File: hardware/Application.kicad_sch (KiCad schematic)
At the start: 0 parts

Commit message: Schematic updates: stm32 sheet
Signed-off-by: Connor Rigby <connorr@hey.com>
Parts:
- added C504, C505: C_0402_DNP, Capacitor_SMD:C_0402_1005Metric, symbol LCSC_Capacitor:C_0402_DNP
- added C505, C507, C50823, C50835, C50848, C511: C_0402_100nf_X7R, Capacitor_SMD:C_0402_1005Metric, symbol LCSC_Capacitor:C_0402_100nf_X7R
- added C509: C_0805_10u_X5R, Capacitor_SMD:C_0805_2012Metric, symbol LCSC_Capacitor:C_0805_10u_X5R
- added R502: R_0402_10k, Resistor_SMD:R_0402_1005Metric, symbol LCSC_Resistor:R_0402_10k
- added U501: STM32G431CBU6, LCSC_Microcontroller:UFQFPN-48_L7.0-W7.0-P0.50-BL-EP, symbol LCSC_Microcontroller:STM32G431CBU6
- added Y501: 32_Mhz, Crystal:Crystal_SMD_3225-4Pin_3.2x2.5mm, symbol LCSC_Crystal:32_Mhz
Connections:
- new net GND: U501.49 (EP)

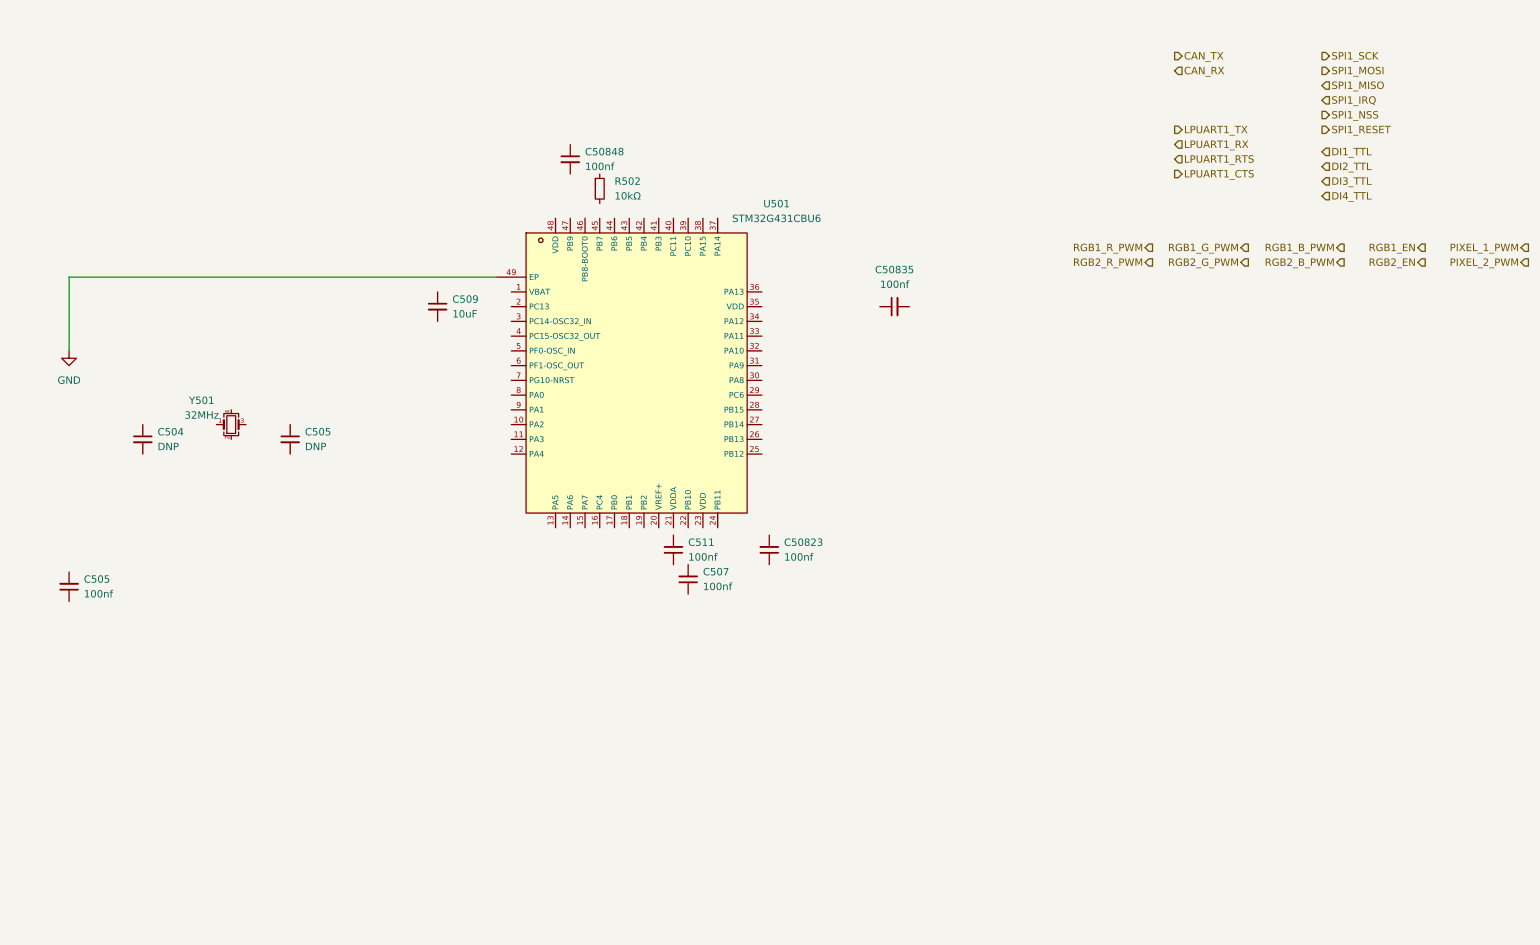
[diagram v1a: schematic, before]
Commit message: Schematic and layout Progress
Signed-off-by: Connor Rigby <connorr@hey.com>
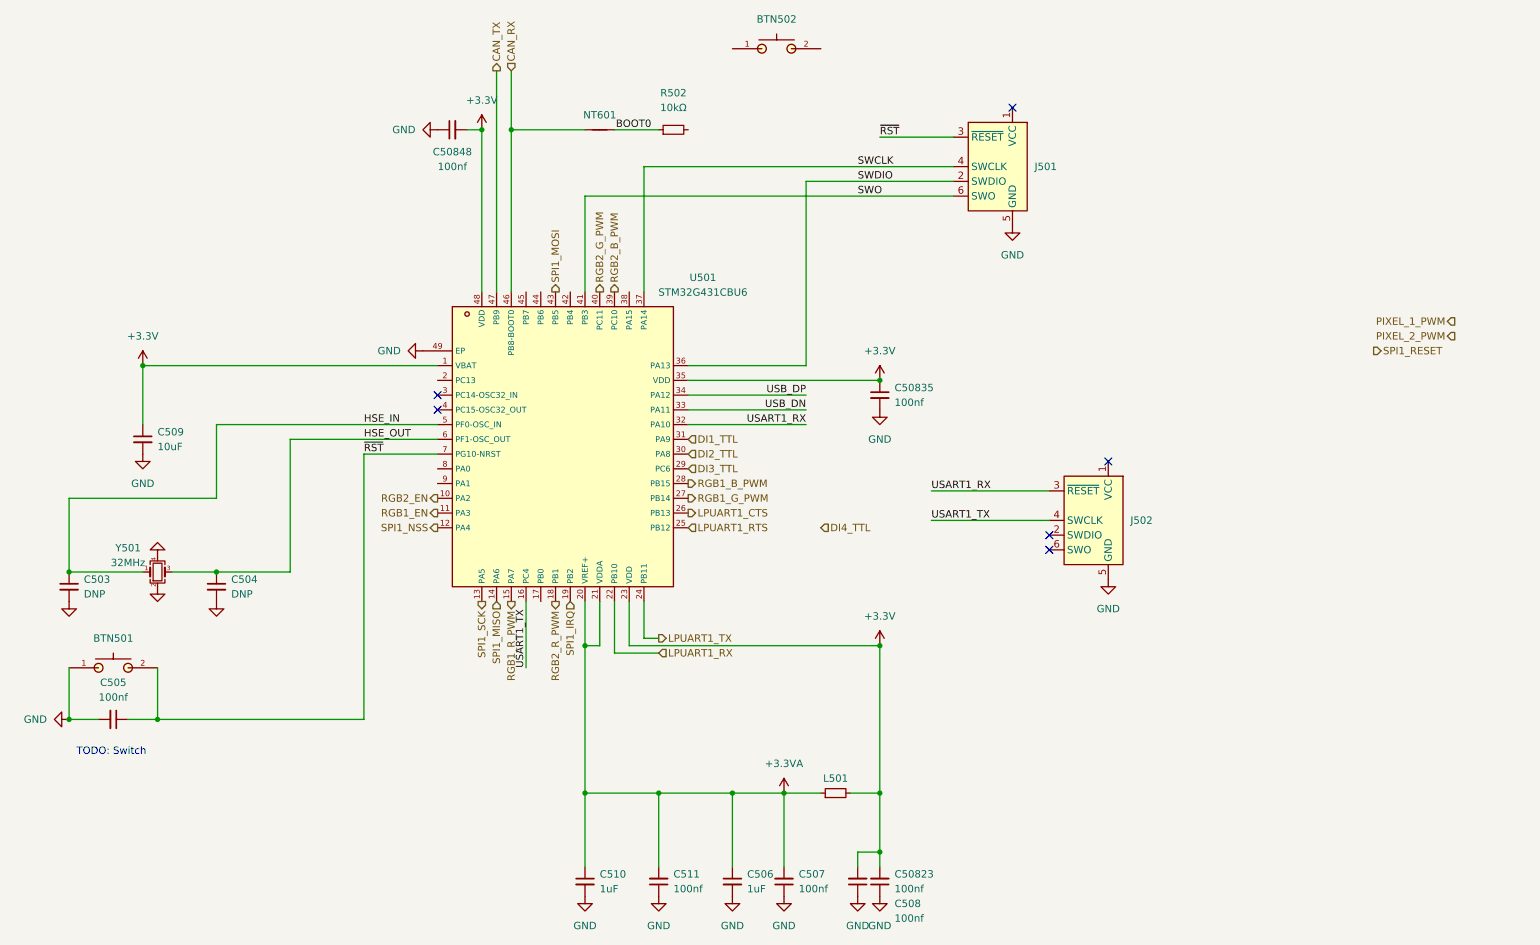
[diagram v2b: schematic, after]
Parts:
- added BTN501, BTN502: GT-TC029B-H025-L1N, Button:SW-SMD_L3.9-W3.0-P4.45, symbol LCSC_Tactile_Switch:GT-TC029B-H025-L1N
- added C506, C510: C_0402_1u_X5R, Capacitor_SMD:C_0402_1005Metric, symbol LCSC_Capacitor:C_0402_1u_X5R
- added C508: C_0402_100nf_X7R, Capacitor_SMD:C_0402_1005Metric, symbol LCSC_Capacitor:C_0402_100nf_X7R
- added J501: Conn_ARM_SWD_TagConnect_TC2030-NL, Connector:Tag-Connect_TC2030-IDC-NL_2x03_P1.27mm_Vertical, symbol Connector:Conn_ARM_SWD_TagConnect_TC2030-NL
- added J502: Conn_ARM_SWD_TagConnect_TC2030, Connector:Tag-Connect_TC2030-IDC-FP_2x03_P1.27mm_Vertical, symbol Connector:Conn_ARM_SWD_TagConnect_TC2030
- added L501: R_0402_DNP, Resistor_SMD:R_0402_1005Metric, symbol LCSC_Resistor:R_0402_DNP
- added NT601: NetTie_2, NetTie:NetTie-2_SMD_Pad0.5mm, symbol Device:NetTie_2
- renumbered C504 to C503, C505 to C504
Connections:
- net CAN_RX: now also U501.46 (PB8-BOOT0), NT601.1
- net CAN_TX: now also U501.47 (PB9)
- net DI1_TTL: now also U501.31 (PA9)
- net DI2_TTL: now also U501.30 (PA8)
- net DI3_TTL: now also U501.29 (PC6)
- net GND: now also C503.2, C504.2, C505.2, C507.1, C50823.1, C50835.2, C50848.1, C509.2, C511.1, Y501.2, Y501.4, BTN501.1, C506.2, C508.1, C510.2, J501.5 (GND), J502.5 (GND)
- net LPUART1_CTS: now also U501.26 (PB13)
- net LPUART1_RTS: now also U501.25 (PB12)
- net LPUART1_RX: now also U501.22 (PB10)
- net LPUART1_TX: now also U501.24 (PB11)
- net RGB1_B_PWM: now also U501.28 (PB15)
- net RGB1_EN: now also U501.11 (PA3)
- net RGB1_G_PWM: now also U501.27 (PB14)
- net RGB1_R_PWM: now also U501.15 (PA7)
- net RGB2_B_PWM: now also U501.39 (PC10)
- net RGB2_EN: now also U501.10 (PA2)
- net RGB2_G_PWM: now also U501.40 (PC11)
- net RGB2_R_PWM: now also U501.18 (PB1)
- net SPI1_IRQ: now also U501.19 (PB2)
- net SPI1_MISO: now also U501.14 (PA6)
- net SPI1_MOSI: now also U501.43 (PB5)
- net SPI1_NSS: now also U501.12 (PA4)
- net SPI1_SCK: now also U501.13 (PA5)
- net HSE_IN: now reaches Y501.1
- net HSE_IN: now also C503.1, U501.5 (PF0-OSC_IN)
- net HSE_OUT: now reaches Y501.3
- net HSE_OUT: now also C504.1, U501.6 (PF1-OSC_OUT)
- net +3.3VA: now reaches C507.2
- net +3.3VA: now also C511.2, U501.20 (VREF+), U501.21 (VDDA), C506.1, C510.1, L501.1
- net +3.3V: now reaches C50823.2
- net +3.3V: now also C50835.1, C50848.2, C509.1, U501.1 (VBAT), U501.23 (VDD), U501.35 (VDD), U501.48 (VDD), C508.2, L501.2
- net USART1_TX: now reaches U501.16 (PC4)
- net USART1_TX: now also J502.4 (SWCLK)
- net USART1_RX: now reaches U501.32 (PA10)
- net USART1_RX: now also J502.3 (~{RESET})
- net USB_DN: now reaches U501.33 (PA11)
- net USB_DP: now reaches U501.34 (PA12)
- net SWDIO: now reaches U501.36 (PA13)
- net SWDIO: now also J501.2 (SWDIO)
- net SWCLK: now reaches U501.37 (PA14)
- net SWCLK: now also J501.4 (SWCLK)
- net SWO: now reaches U501.41 (PB3)
- net SWO: now also J501.6 (SWO)
- net ~{RST}: now reaches U501.7 (PG10-NRST)
- net ~{RST}: now also C505.1, BTN501.2, J501.3 (~{RESET})
- net BOOT0: now reaches R502.1
- net BOOT0: now also NT601.2
- no-connect marks 0 -> 6
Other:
- note added: "TODO: Switch"
- moved on the sheet: C503, C504, C505, C507, C50823, C50835, C50848, C509, C511, R502, U501, Y501

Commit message: Layout updates
Signed-off-by: Connor Rigby <connorr@hey.com>
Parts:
- added R501: R_0402_1k, Resistor_SMD:R_0402_1005Metric, symbol LCSC_Resistor:R_0402_1k
- added TP501: DP, TestPoint:TestPoint_Pad_D1.0mm, symbol Connector:TestPoint
- added TP502: DN, TestPoint:TestPoint_Pad_D1.0mm, symbol Connector:TestPoint
- added TP503: GND, TestPoint:TestPoint_Pad_D1.0mm, symbol Connector:TestPoint
- U501: footprint LCSC_Microcontroller:UFQFPN-48_L7.0-W7.0-P0.50-BL-EP -> LCSC_Microcontroller:QFN50P700X700X60-49N
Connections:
- net +3.3V: now also R501.2
- net BOOT0: now also BTN502.1
- net DI1_TTL: now also U501.29 (PC6); no longer U501.31 (PA9)
- net DI3_TTL: now also U501.31 (PA9); no longer U501.29 (PC6)
- net DI4_TTL: now also U501.38 (PA15)
- net GND: now also R502.2, TP503.1
- net PIXEL_1_PWM: now also U501.42 (PB4)
- net SPI1_RESET: now also U501.17 (PB0)
- net USB_DN: now also TP502.1
- net USB_DP: now also TP501.1
- net at BTN502.2: now also R501.1
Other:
- note removed: "TODO: Switch"
- moved on the sheet: BTN502, J502, R502

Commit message: Update layout
Signed-off-by: Connor Rigby <connorr@hey.com>
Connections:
- net PIXEL_2_PWM: now also U501.9 (PA1)
- no-connect marks 6 -> 9
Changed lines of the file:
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@@
   )
   (no_connect (at 231.14 34.29))
+  (no_connect (at 104.14 66.04))
+  (no_connect (at 88.9 96.52))
   (no_connect (at 220.98 46.99))
   (no_connect (at 187.96 34.29))
+  (no_connect (at 106.68 66.04))
   (no_connect (at 88.9 83.82))
   (no_connect (at 220.98 49.53))
@@
     (stroke (width 0) (type default))
   )
-  (wire (pts (xy 50.8 88.9) (xy 50.8 101.6))
+  (wire (pts (xy 50.8 88.9) (xy 50.8 102.87))
     (stroke (width 0) (type default))
   )
@@
     (stroke (width 0) (type default))
   )
-  (wire (pts (xy 76.2 139.7) (xy 40.64 139.7))
+  (wire (pts (xy 58.42 139.7) (xy 40.64 139.7))
     (stroke (width 0) (type default))
   )
@@
     (stroke (width 0) (type default))
   )
-  (wire (pts (xy 25.4 101.6) (xy 50.8 101.6))
+  (wire (pts (xy 25.4 102.87) (xy 50.8 102.87))
     (stroke (width 0) (type default))
   )
@@
     (stroke (width 0) (type default))
   )
-  (wire (pts (xy 88.9 93.98) (xy 76.2 93.98))
+  (wire (pts (xy 88.9 93.98) (xy 58.42 93.98))
     (stroke (width 0) (type default))
   )
@@
     (stroke (width 0) (type default))
   )
-  (wire (pts (xy 76.2 93.98) (xy 76.2 139.7))
-    (stroke (width 0) (type default))
-  )
-  (wire (pts (xy 63.5 91.44) (xy 88.9 91.44))
+  (wire (pts (xy 58.42 93.98) (xy 58.42 139.7))
+    (stroke (width 0) (type default))
+  )
+  (wire (pts (xy 54.61 91.44) (xy 88.9 91.44))
     (stroke (width 0) (type default))
   )
@@
     (stroke (width 0) (type default))
   )
-  (wire (pts (xy 25.4 114.3) (xy 25.4 101.6))
-    (stroke (width 0) (type default))
-  )
-  (wire (pts (xy 63.5 114.3) (xy 63.5 91.44))
+  (wire (pts (xy 25.4 114.3) (xy 25.4 102.87))
+    (stroke (width 0) (type default))
+  )
+  (wire (pts (xy 54.61 114.3) (xy 54.61 91.44))
     (stroke (width 0) (type default))
   )
@@
     (stroke (width 0) (type default))
   )
-  (wire (pts (xy 63.5 114.3) (xy 50.8 114.3))
+  (wire (pts (xy 54.61 114.3) (xy 50.8 114.3))
     (stroke (width 0) (type default))
   )
@@
     (effects (font (size 1.27 1.27)) (justify left))
   )
-  (hierarchical_label "PIXEL_2_PWM" (shape output) (at 86.36 146.05 180) (fields_autoplaced)
+  (hierarchical_label "PIXEL_2_PWM" (shape output) (at 88.9 99.06 180) (fields_autoplaced)
     (effects (font (size 1.27 1.27)) (justify right))
   )

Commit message: Almost ready for fab
Signed-off-by: Connor Rigby <connorr@hey.com>
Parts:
- removed C503, C504: C_0402_DNP, Capacitor_SMD:C_0402_1005Metric, symbol LCSC_Capacitor:C_0402_DNP
- removed L501: R_0402_DNP, Resistor_SMD:R_0402_1005Metric, symbol LCSC_Resistor:R_0402_DNP
- added C503, C504: C_0402_33p_C0G, Capacitor_SMD:C_0402_1005Metric, symbol LCSC_Capacitor:C_0402_33p_C0G
- added D501: LED_0603_GREEN, LED_SMD:LED_0603_1608Metric, symbol LCSC_LED:LED_0603_GREEN
- added D502: LED_0603_YELLOW, LED_SMD:LED_0603_1608Metric, symbol LCSC_LED:LED_0603_YELLOW
- added L501: R_0402_0, Resistor_SMD:R_0402_1005Metric, symbol LCSC_Resistor:R_0402_0
- added R503, R504: R_0603_330, Resistor_SMD:R_0603_1608Metric, symbol LCSC_Resistor:R_0603_330
- J501: now left out of the parts list
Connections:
- net +3.3V: now also D501.2 (A), D502.2 (A), L501.2
- net +3.3VA: now also L501.1
- net GND: now also C503.2, C504.2
- net HSE_IN: now also C503.1
- net HSE_OUT: now also C504.1
- net LED_GREEN: now reaches U501.44 (PB6)
- net LED_GREEN: now also R503.2
- net LED_YELLOW: now reaches U501.45 (PB7)
- net LED_YELLOW: now also R504.2
- new net LED_GREEN_CSR: D501.1 (K), R503.1
- new net LED_YELLOW_CSR: D502.1 (K), R504.1
- no-connect marks 9 -> 8
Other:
- note added: "CL = ((CX1 x CX2) / (CX1 + CX2)) + Cstray CX1 = CX2 = 2(CL - Cstray) 33pf = CX2 = 2(22pf - 2pf)"
- moved on the sheet: BTN501, C505, C509, R502

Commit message: Pre-production updates
Signed-off-by: Connor Rigby <connorr@hey.com>
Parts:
- TP501, TP502, TP503: now left out of the parts list
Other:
- company: (none) -> https://cone.codes
- title: (none) -> coneRGB2
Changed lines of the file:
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@@
 (kicad_sch (version 20230121) (generator eeschema)
   (paper "A4")
+  (title_block
+    (title "coneRGB2")
+    (date "2023-03-20")
+    (rev "1")
+    (company "https://cone.codes")
+    (comment 1 "https://github.com/connorrigby/underglow2")
+    (comment 2 "Designed by Connor Rigby")
+    (comment 3 "Main microcontroller handles all core functionality of the device")
+    (comment 4 "STM32G4 Microcontroller")
+  )
   (junction (at 25.4 50.8) (diameter 0) (color 0 0 0 0)
   )
@@
   )
   (symbol (lib_id "Connector:TestPoint") (at 171.45 90.17 180) (unit 1)
-    (in_bom yes) (on_board yes) (dnp no)
+    (in_bom no) (on_board yes) (dnp no)
     (property "Reference" "TP503" (at 168.91 96.52 0)
       (effects (font (size 1.27 1.27)) (justify right))
@@
   )
   (symbol (lib_id "Connector:TestPoint") (at 160.02 90.17 180) (unit 1)
-    (in_bom yes) (on_board yes) (dnp no)
+    (in_bom no) (on_board yes) (dnp no)
     (property "Reference" "TP501" (at 157.48 96.52 0)
       (effects (font (size 1.27 1.27)) (justify right))
@@
   )
   (symbol (lib_id "Connector:TestPoint") (at 153.67 90.17 180) (unit 1)
-    (in_bom yes) (on_board yes) (dnp no)
+    (in_bom no) (on_board yes) (dnp no)
     (property "Reference" "TP502" (at 151.13 96.52 0)
       (effects (font (size 1.27 1.27)) (justify right))

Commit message: More pre-production updates:
* fix USART connections being reversed
* add test points for SPI and BLE

Signed-off-by: Connor Rigby <connorr@hey.com>
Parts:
- removed NT601: NetTie_2, NetTie:NetTie-2_SMD_Pad0.5mm, symbol Device:NetTie_2
- added J503: BOOT0, Connector_PinHeader_2.54mm:PinHeader_1x02_P2.54mm_Vertical, symbol Connector_Generic:Conn_01x02
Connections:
- net BOOT0: now also J503.2 (Pin_2)
- net CAN_RX: now also J503.1 (Pin_1)
- net USART1_RX: now also J502.4 (SWCLK); no longer J502.3 (~{RESET})
- net USART1_TX: now also J502.3 (~{RESET}); no longer J502.4 (SWCLK)
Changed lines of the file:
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@@
+    (stroke (width 0) (type default))
+  )
+  (wire (pts (xy 115.57 34.29) (xy 115.57 38.1))
     (stroke (width 0) (type default))
   )
@@
     (stroke (width 0) (type default))
   )
-  (wire (pts (xy 114.3 38.1) (xy 101.6 38.1))
+  (wire (pts (xy 101.6 38.1) (xy 115.57 38.1))
     (stroke (width 0) (type default))
   )
@@
     (stroke (width 0) (type default))
   )
-  (wire (pts (xy 220.98 39.37) (xy 200.66 39.37))
+  (wire (pts (xy 220.98 44.45) (xy 200.66 44.45))
     (stroke (width 0) (type default))
   )
@@
     (stroke (width 0) (type default))
   )
+  (wire (pts (xy 118.11 34.29) (xy 118.11 38.1))
+    (stroke (width 0) (type default))
+  )
   (wire (pts (xy 119.38 119.38) (xy 119.38 128.27))
     (stroke (width 0) (type default))
@@
     (stroke (width 0) (type default))
   )
-  (wire (pts (xy 200.66 44.45) (xy 220.98 44.45))
+  (wire (pts (xy 200.66 39.37) (xy 220.98 39.37))
     (stroke (width 0) (type default))
   )
@@
     (stroke (width 0) (type default))
   )
-  (wire (pts (xy 119.38 38.1) (xy 127 38.1))
+  (wire (pts (xy 118.11 38.1) (xy 127 38.1))
     (stroke (width 0) (type default))
   )
@@
     )
   )
-  (label "USART1_RX" (at 200.66 39.37 0) (fields_autoplaced)
+  (label "USART1_RX" (at 200.66 44.45 0) (fields_autoplaced)
+    (effects (font (size 1.27 1.27)) (justify left bottom))
+    (property "Netclass" "UART" (at 200.66 45.72 0)
+      (effects (font (size 1.27 1.27) italic) (justify left) hide)
+    )
+  )
+  (label "USART1_TX" (at 200.66 39.37 0) (fields_autoplaced)
     (effects (font (size 1.27 1.27)) (justify left bottom))
     (property "Netclass" "UART" (at 200.66 40.64 0)
-      (effects (font (size 1.27 1.27) italic) (justify left) hide)
-    )
-  )
-  (label "USART1_TX" (at 200.66 44.45 0) (fields_autoplaced)
-    (effects (font (size 1.27 1.27)) (justify left bottom))
-    (property "Netclass" "UART" (at 200.66 45.72 0)
       (effects (font (size 1.27 1.27) italic) (justify left) hide)
     )
@@
     )
   )
-  (symbol (lib_id "Device:NetTie_2") (at 116.84 38.1 0) (unit 1)
-    (in_bom no) (on_board yes) (dnp no)
-    (property "Reference" "NT601" (at 116.84 36.83 0)
-      (effects (font (size 1.27 1.27)))
-    )
-    (property "Value" "NetTie_2" (at 116.84 35.56 0)
-      (effects (font (size 1.27 1.27)) hide)
-    )
-    (property "Footprint" "NetTie:NetTie-2_SMD_Pad0.5mm" (at 116.84 38.1 0)
-      (effects (font (size 1.27 1.27)) hide)
-    )
-    (property "Datasheet" "~" (at 116.84 38.1 0)
-      (effects (font (size 1.27 1.27)) hide)
-    )
-    (pin "1")
-    (pin "2")
-    (instances
-      (project "underglow2"
-        (path "/dcbdf88a-d6ac-4b1d-9514-0b0ce113d90b/f11066f7-65e1-4360-b792-c6d8a0045fba"
-          (reference "NT601") (unit 1)
-        )
-      )
-    )
-  )
   (symbol (lib_id "power:+3.3V") (at 152.4 25.4 270) (unit 1)
     (in_bom yes) (on_board yes) (dnp no)
@@
         )
       )
+    )
+  )
+  (symbol (lib_id "Connector_Generic:Conn_01x02") (at 115.57 29.21 90) (unit 1)
+    (in_bom no) (on_board yes) (dnp yes)
+    (property "Reference" "J503" (at 114.3 23.495 90)
+      (effects (font (size 1.27 1.27)) (justify right))
+    )
+    (property "Value" "BOOT0" (at 114.3 26.035 90)
+      (effects (font (size 1.27 1.27)) (justify right))
+    )
+    (property "Footprint" "Connector_PinHeader_2.54mm:PinHeader_1x02_P2.54mm_Vertical" (at 115.57 29.21 0)
+      (effects (font (size 1.27 1.27)) hide)
+    )
+    (property "Datasheet" "~" (at 115.57 29.21 0)
+      (effects (font (size 1.27 1.27)) hide)
+    )
+    (pin "1")
+    (pin "2")
+    (instances
+      (project "underglow2"
+        (path "/dcbdf88a-d6ac-4b1d-9514-0b0ce113d90b/f11066f7-65e1-4360-b792-c6d8a0045fba"
+          (reference "J503") (unit 1)
+        )
+      )
